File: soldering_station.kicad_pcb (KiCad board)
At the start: 2 copper layers, 68 parts, among them IC1 ATMEGA8A-P, J1 Heat gun, P1 17v, P2 220v, P3 24v|220v, P4 solder, P5 thermocouple, Q1 КТ313Б, Q2 КТ313Б, Q3 КТ313Б, Q4 КТ815А, SW1 mode, SW2 Enc, U1 TL072, U2 MOC3023M, U3 MOC3023M, U4 LM7805CT, Y1 16.000

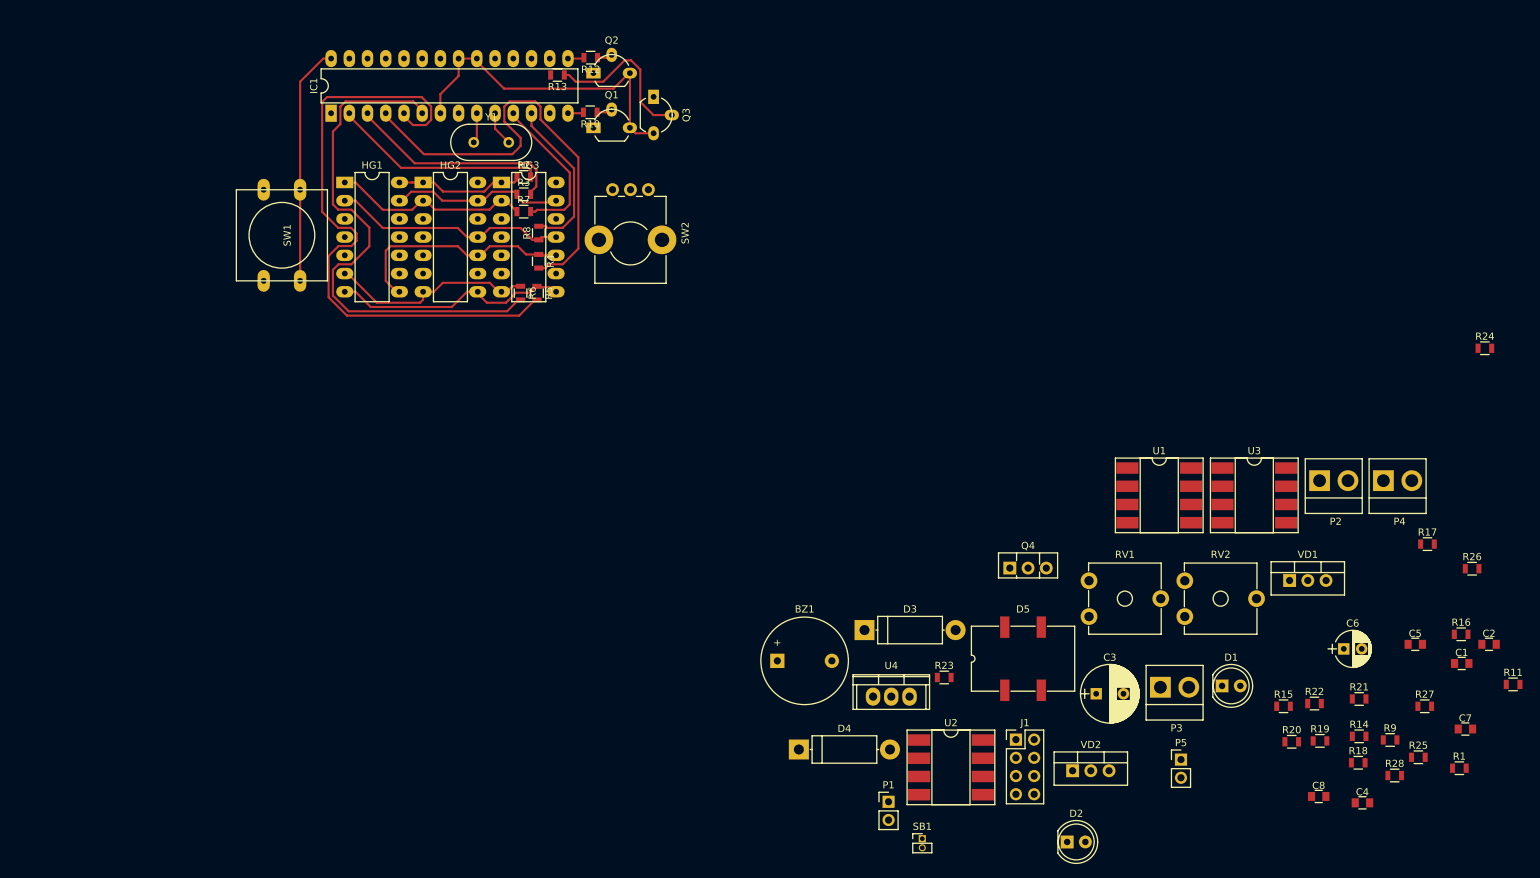
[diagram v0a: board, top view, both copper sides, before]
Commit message: Change heater gun connector
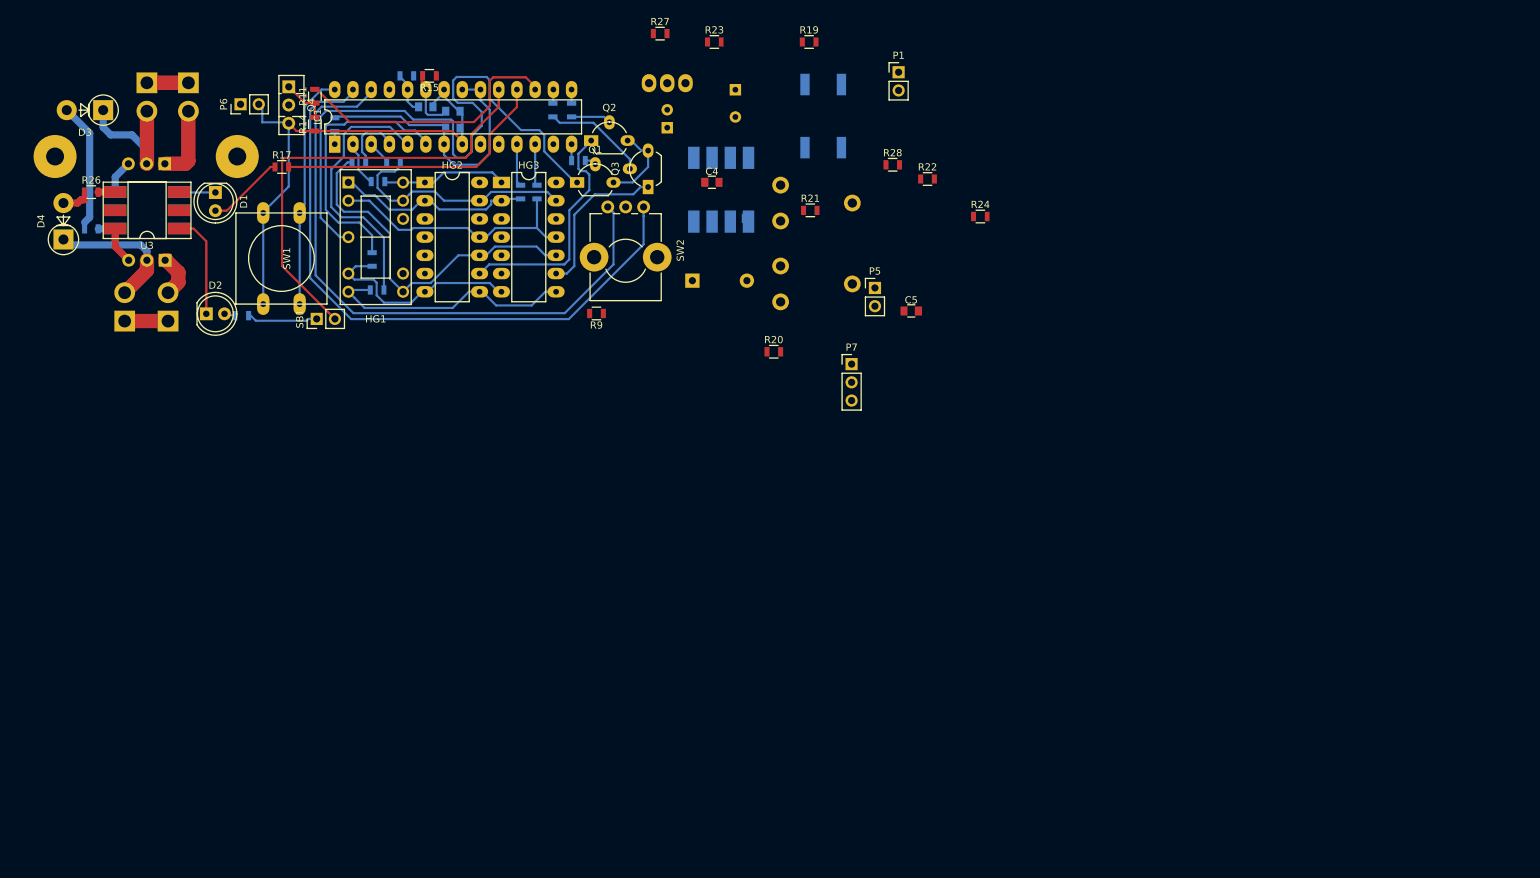
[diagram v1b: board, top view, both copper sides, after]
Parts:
- removed J1: Heat gun, Pin_Headers:Pin_Header_Straight_2x04_Pitch2.54mm
- removed Y1: 16.000, Crystals:Crystal_HC49-U_Vertical
- added P6: Fan, Pin_Headers:Pin_Header_Straight_1x02_Pitch2.54mm, F.Cu at (91.1, 47.7)
- added P7: thermocouple, Pin_Headers:Pin_Header_Straight_1x03_Pitch2.54mm, F.Cu at (176.3, 83.9)
- added P8: Heater, Pin_Headers:Pin_Header_Straight_1x02_Pitch3.96mm_Friction_Lock, B.Cu at (83.9, 44.7)
- added REF**: Heatsink_Fischer_SK104-STC-STIC_35x13mm_2xDrill2.5mm, Heatsinks:Heatsink_Fischer_SK104-STC-STIC_35x13mm_2xDrill2.5mm, B.Cu at (78.0, 54.9)
- BZ1, C1, C2, C3, C6, C7, C8, D5, P2, P3, P4, R1, R10, R12, R13, R16, R18, R2, R25, R3, R4, R5, R6, R7, R8, RV1, RV2, U1, U4, VD1, VD2: moved to B.Cu
- D3, D4: footprint Diodes_ThroughHole:D_5W_P12.70mm_Horizontal -> Diodes_THT:D_5W_P5.08mm_Vertical_AnodeUp
- HG1: footprint Housings_DIP:DIP-14_W7.62mm_LongPads -> Displays_7-Segment:MAN3640A
- SB1: footprint Pin_Headers:Pin_Header_Straight_1x02_Pitch1.27mm -> Pin_Headers:Pin_Header_Straight_1x02_Pitch2.54mm
- U2: footprint Housings_DIP:DIP-8_W8.89mm_SMDSocket_LongPads -> Housings_DIP:DIP-6_W8.89mm_SMDSocket_LongPads; moved to B.Cu
- U3: footprint Housings_DIP:DIP-8_W8.89mm_SMDSocket_LongPads -> Housings_DIP:DIP-6_W8.89mm_SMDSocket_LongPads
- moved R26 199.5 mm to (70.3, 59.9)
- moved R25 199.1 mm to (70.3, 65.0)
- moved R11 186.1 mm to (101.5, 46.5), turned to 90 degrees
- moved R1 180.6 mm to (104.3, 50.5), turned to 90 degrees
- moved P2 172.6 mm to (78.1, 44.7), turned to 270 degrees
- moved P4 170.9 mm to (81.0, 77.9), turned to 90 degrees
- moved R14 168.7 mm to (101.5, 50.4), turned to 90 degrees
- moved R17 168.1 mm to (96.9, 56.4)
- moved R18 167.7 mm to (91.3, 77.1)
- moved VD1 167.2 mm to (80.6, 55.9), turned to 180 degrees
- moved R16 166.3 mm to (114.3, 43.7), turned to 180 degrees
- moved C2 166.1 mm to (117.0, 48.0)
- moved C7 164.2 mm to (120.7, 51.0)
- moved C1 160.3 mm to (120.7, 48.6)
- moved U3 159.4 mm to (78.1, 62.4), turned to 180 degrees
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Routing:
- net Net-(IC1-Pad27): track 0.00 -> 89.2 mm
- net Net-(IC1-Pad26): track 0.00 -> 86.9 mm
- net Net-(P2-Pad1): track 0.00 -> 75.4 mm
- net GND: track 0.00 -> 70.3 mm
- net Net-(IC1-Pad19): track 0.00 -> 62.7 mm
- net Net-(IC1-Pad4): track 62.6 -> 8.91 mm
- net Net-(IC1-Pad5): track 86.8 -> 37.6 mm
- net Net-(IC1-Pad18): track 0.00 -> 39.3 mm
- net Net-(IC1-Pad17): track 0.00 -> 38.6 mm
- net Net-(IC1-Pad6): track 73.5 -> 38.1 mm
- net Net-(HG2-Pad9): track 0.00 -> 32.8 mm
- net Net-(HG1-Pad4): track 0.00 -> 30.1 mm
- net Net-(IC1-Pad3): track 30.8 -> 3.44 mm
- net Net-(IC1-Pad2): track 29.7 -> 6.73 mm
- net Net-(HG3-Pad9): track 0.00 -> 22.0 mm
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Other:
- net class 1mm added: clearance 1, trace_width 1, via_dia 1.1, via_drill 0.7
- net class Default: via_dia 0.8 -> 0.85; via_drill 0.4 -> 0.5

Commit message: Fix
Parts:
- C8, D5, U1: moved to F.Cu
- moved R19 31.5 mm to (159.5, 68.5)
- moved R24 31.3 mm to (163.0, 64.8), turned to 180 degrees
- moved C5 23.6 mm to (163.2, 66.6)
- moved R22 20.4 mm to (168.1, 65.8), turned to 180 degrees
- moved BZ1 18.0 mm to (171.7, 76.3), turned to 90 degrees
- moved R23 17.8 mm to (150.9, 55.6), turned to 270 degrees
- moved P7 17.5 mm to (159.9, 77.9), turned to 270 degrees
- moved R28 14.0 mm to (170.3, 63.7), turned to 180 degrees
- moved R20 13.8 mm to (163.0, 68.5)
- moved R27 13.4 mm to (147.3, 51.0), turned to 270 degrees
- moved RV1 13.0 mm to (153.5, 68.6)
- moved P5 10.1 mm to (179.9, 63.1)
- moved R9 9.87 mm to (150.6, 76.9), turned to 270 degrees
- moved C4 6.47 mm to (150.9, 61.0), turned to 270 degrees
- moved P1 6.08 mm to (180.0, 48.5)
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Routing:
- net GND: track 70.3 -> 389.0 mm, vias 0 -> 1
- net +5V: track 51.3 -> 244.0 mm, vias 0 -> 1
- net Net-(IC1-Pad25): track 7.88 -> 130.6 mm
- net +24V: track 0.00 -> 81.5 mm
- net Net-(P2-Pad1): track 75.4 -> 5.79 mm
- net Net-(R16-Pad1): track 0.00 -> 62.2 mm
- net Net-(R15-Pad1): track 0.00 -> 59.8 mm
- net Net-(HG1-Pad4): track 30.1 -> 86.0 mm
- net Net-(IC1-Pad13): track 0.00 -> 49.3 mm
- net Net-(P7-Pad1): track 3.79 -> 42.7 mm
- net Net-(P5-Pad1): track 0.00 -> 27.0 mm
- net Net-(BZ1-Pad1): track 0.00 -> 21.7 mm
- net Net-(R19-Pad1): track 0.00 -> 17.9 mm
- net Net-(R21-Pad1): track 0.00 -> 17.7 mm
- net Net-(R19-Pad2): track 0.00 -> 16.8 mm
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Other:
- board outline added: 121 x 38.4 mm

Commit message: Add 3D view
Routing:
- net (no net): track 0.00 -> 81.5 mm
- net GND: track 389.0 -> 423.3 mm, vias 1 -> 2
- net +5V: track 244.0 -> 261.8 mm
- net Net-(HG1-Pad4): track 86.0 -> 88.9 mm
- added copper zone on B.Cu, net GND
- added copper zone on F.Cu, net GND

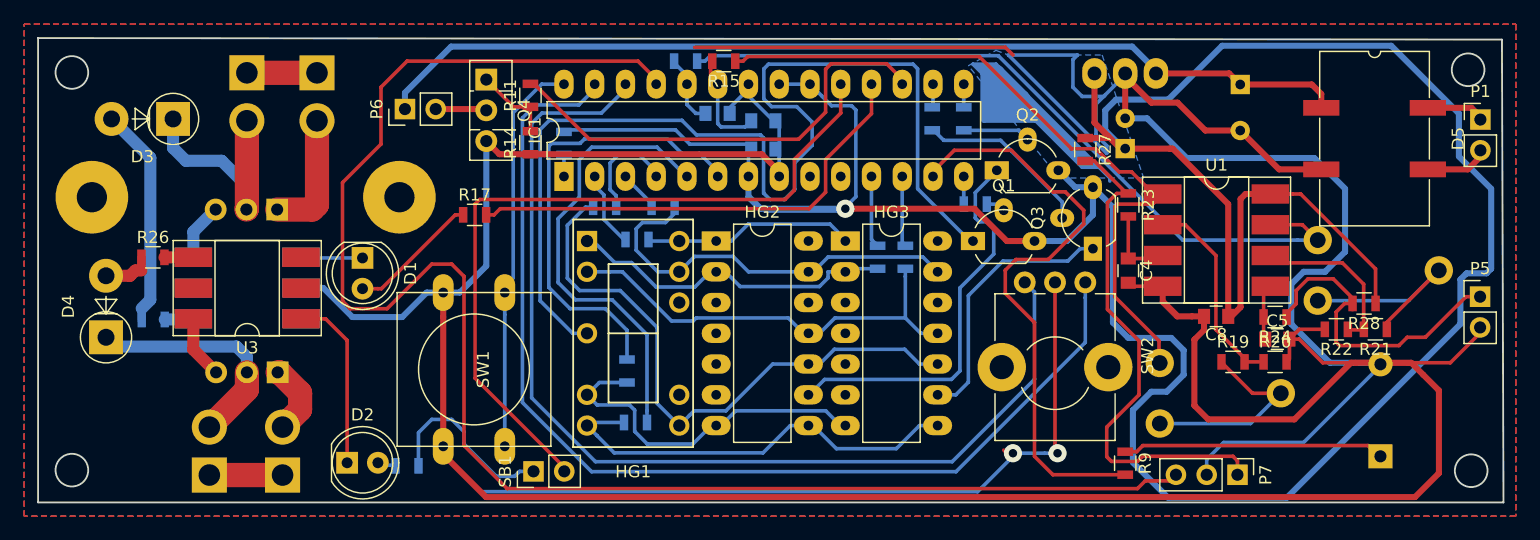
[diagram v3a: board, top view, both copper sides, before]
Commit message: Fix ADC ref pin
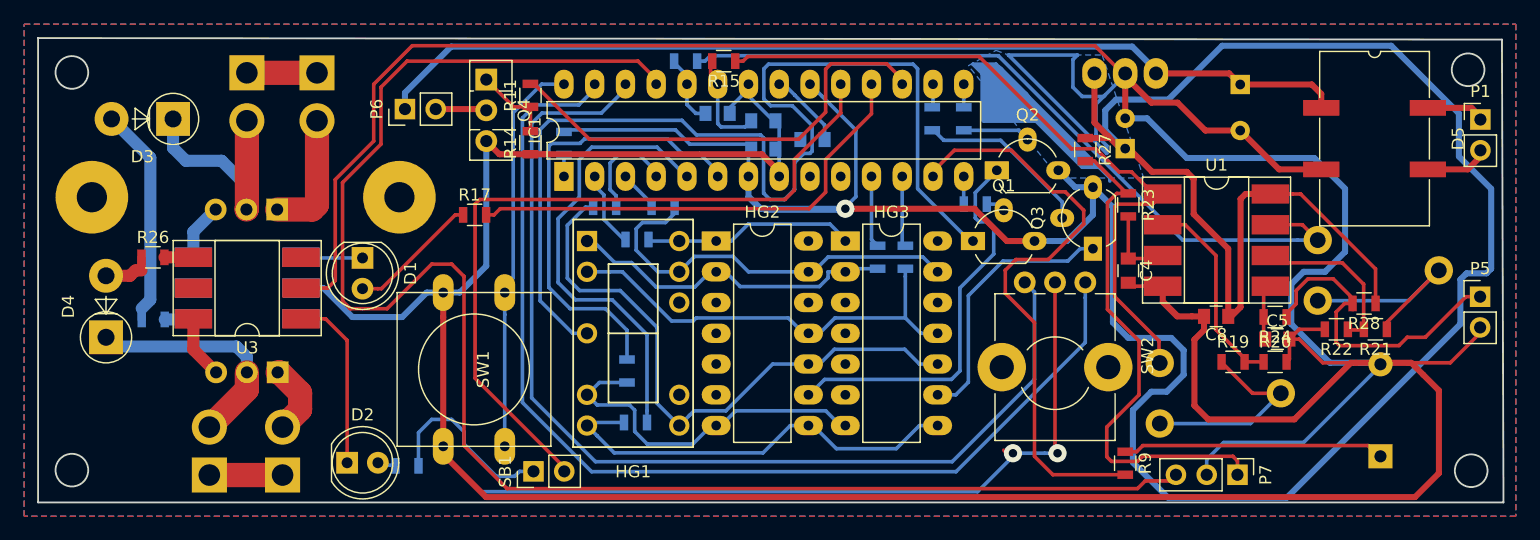
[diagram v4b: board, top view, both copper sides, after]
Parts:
- added C9: 0.1, Capacitors_SMD:C_0805, B.Cu at (124.8, 50.2)
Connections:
- IC1 pad 21: +5V -> Net-(C9-Pad1)
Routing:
- net GND: track 423.3 -> 508.5 mm
- net (no net): track 81.5 -> 55.0 mm
- net Net-(C9-Pad1): track 0.00 -> 5.84 mm
- net +5V: track 261.8 -> 257.9 mm

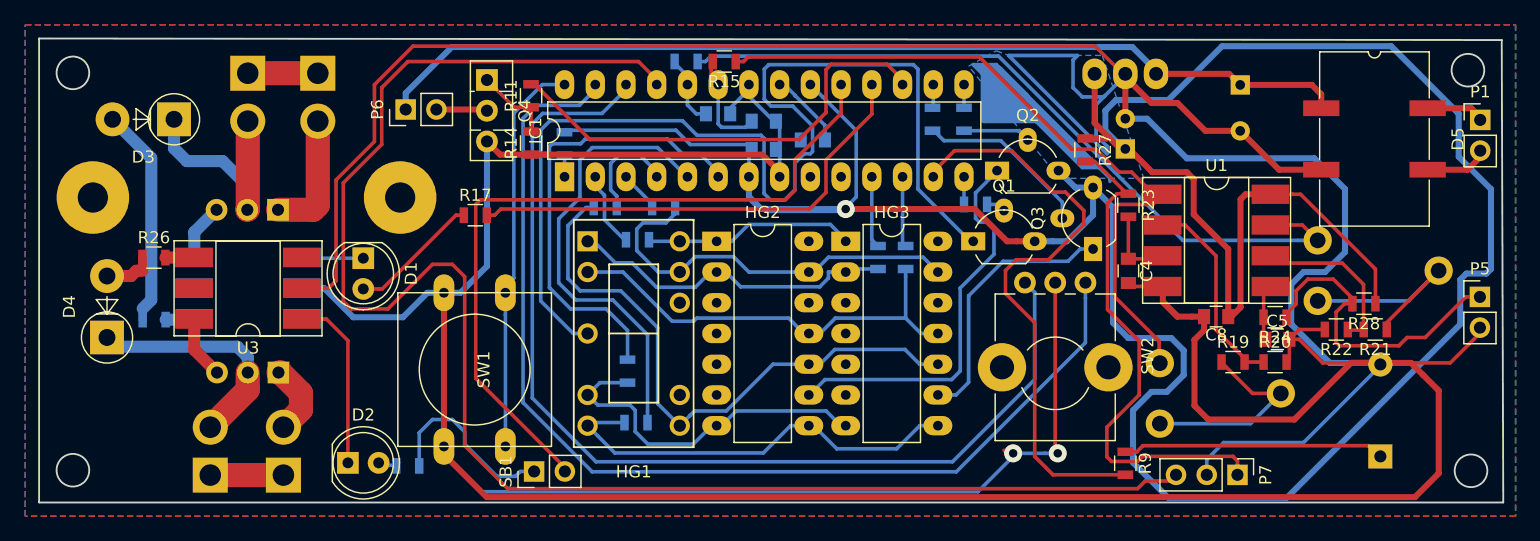
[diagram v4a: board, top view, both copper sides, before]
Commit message: Fix encoder
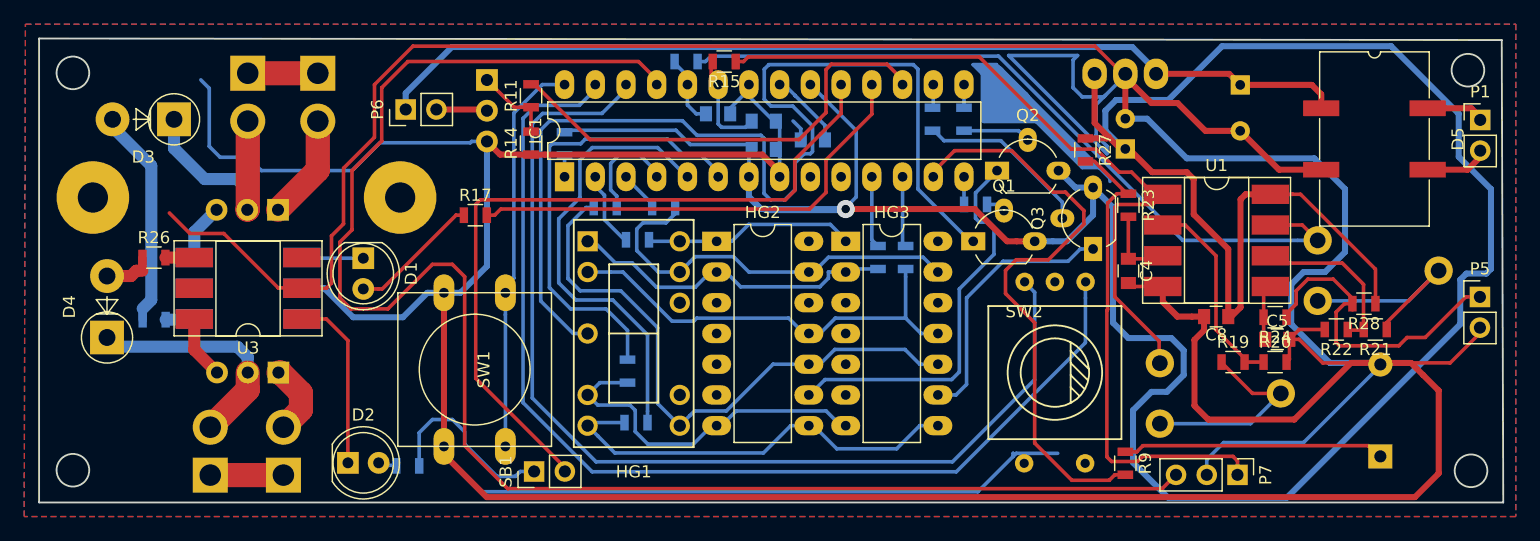
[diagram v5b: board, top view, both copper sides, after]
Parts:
- Q4: moved to B.Cu
- SW2: footprint Potentiometers:Potentiometer_Alps_RK09K_Horizontal -> lib:Encoder_with_button
- moved SW2 5.52 mm to (144.8, 66.9), turned to 0 degrees
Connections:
- U2 pad 3: (no net) -> Net-(U2-Pad3)
- U2 pad 5: (no net) -> Net-(U2-Pad5)
- U3 pad 3: (no net) -> Net-(U3-Pad3)
- U3 pad 5: (no net) -> Net-(U3-Pad5)
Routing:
- net GND: track 508.5 -> 539.3 mm, vias 2 -> 0
- net Net-(P7-Pad1): track 42.7 -> 40.5 mm
- net Net-(P8-Pad2): track 10.4 -> 8.69 mm
- net Net-(D3-Pad2): track 18.2 -> 18.7 mm
